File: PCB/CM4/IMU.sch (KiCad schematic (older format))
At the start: 1 part, among them U1 MPU6050

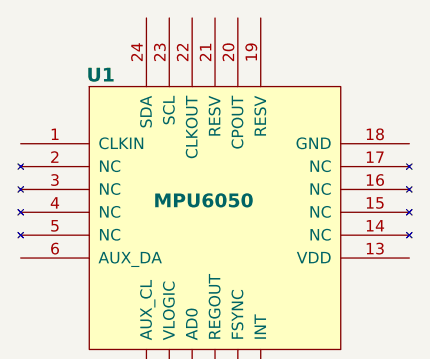
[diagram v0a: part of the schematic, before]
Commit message: Cortex M4 hasbeen placed, decoupling Caps too
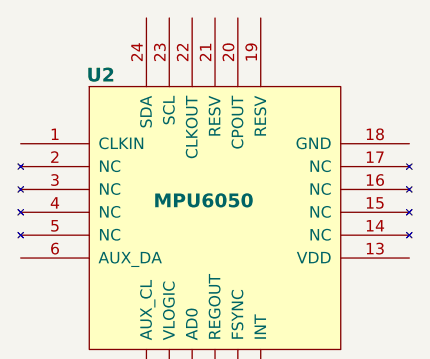
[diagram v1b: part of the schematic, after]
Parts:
- renumbered U1 to U2
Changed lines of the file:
@@
-EESchema Schematic File Version 2  date Fri 02 Nov 2012 01:03:51 PM COT
+EESchema Schematic File Version 2  date Sat 03 Nov 2012 06:00:55 PM COT
 LIBS:power
 LIBS:device
@@
 LIBS:mpu6050
 LIBS:stm32f100vxx
-EELAYER 43  0
+LIBS:HackBo_DroneCore_CM4-cache
+EELAYER 25  0
 EELAYER END
 $Descr A4 11693 8268
 encoding utf-8
-Sheet 2 2
+Sheet 2 3
 Title ""
-Date "2 nov 2012"
+Date "3 nov 2012"
 Rev ""
 Comp ""
@@
 $EndDescr
 $Comp
-L MPU6050 U1
+L MPU6050 U2
 U 1 1 50940AF0
 P 5400 3400
-F 0 "U1" H 4950 3950 60  0000 C CNB
+F 0 "U2" H 4950 3950 60  0000 C CNB
 F 1 "MPU6050" H 5400 3400 60  0000 C CNB
 F 2 "QFN24P" H 5400 3400 60  0001 C CNN

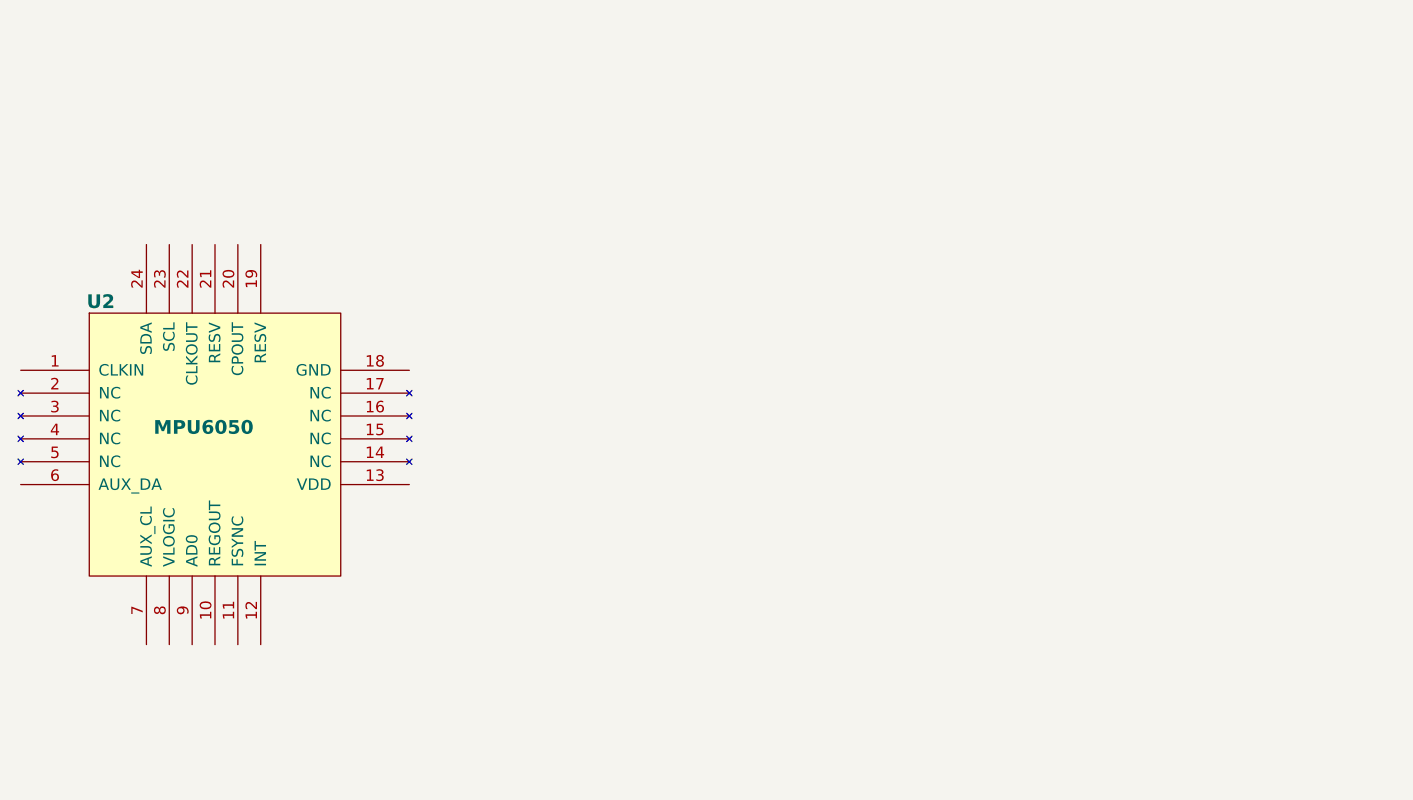
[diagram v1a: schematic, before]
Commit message: IMU caps decoupling
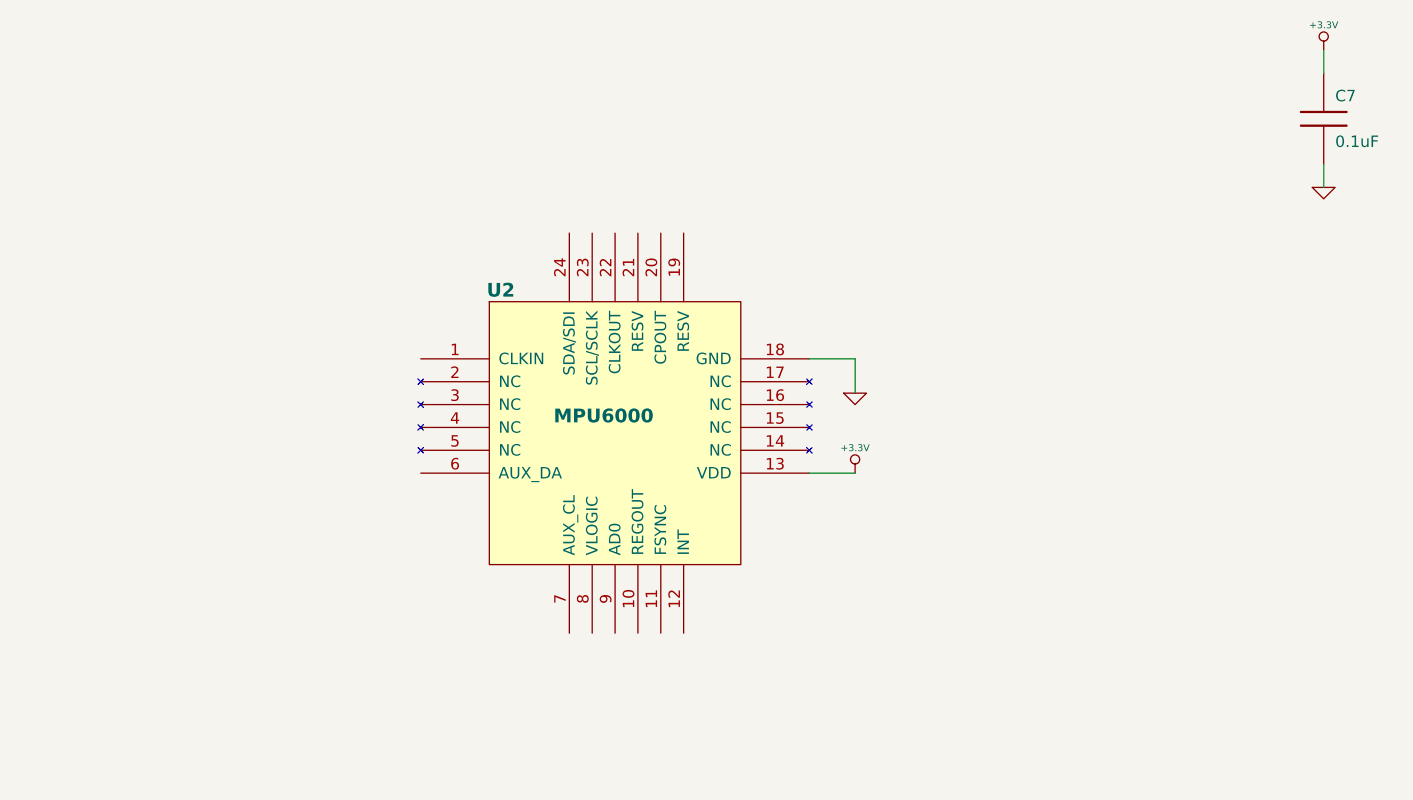
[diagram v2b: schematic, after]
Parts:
- removed U2: MPU6050, QFN24P, symbol MPU6050
- added C7: 0.1uF, 0603, symbol C
- added U2: MPU6000, QFN24P, symbol MPU6000
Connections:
- new net +3.3V: C7.1, U2.13 (VDD)
- new net GND: C7.2, U2.18 (GND)
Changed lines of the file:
@@
-EESchema Schematic File Version 2  date Sat 03 Nov 2012 06:00:55 PM COT
+EESchema Schematic File Version 2  date Sat 03 Nov 2012 06:26:30 PM COT
 LIBS:power
 LIBS:device
@@
 LIBS:mpu6050
 LIBS:stm32f100vxx
+LIBS:mpu6000
 LIBS:HackBo_DroneCore_CM4-cache
 EELAYER 25  0
@@
 $EndDescr
 $Comp
-L MPU6050 U2
-U 1 1 50940AF0
-P 5400 3400
-F 0 "U2" H 4950 3950 60  0000 C CNB
-F 1 "MPU6050" H 5400 3400 60  0000 C CNB
-F 2 "QFN24P" H 5400 3400 60  0001 C CNN
-	1    5400 3400
+L MPU6000 U2
+U 1 1 5095AB32
+P 7150 3350
+F 0 "U2" H 6700 3900 60  0000 C CNB
+F 1 "MPU6000" H 7150 3350 60  0000 C CNB
+F 2 "QFN24P" H 7150 3350 60  0001 C CNN
+	1    7150 3350
 	1    0    0    -1
 $EndComp
+$Comp
+L +3.3V #PWR2
+U 1 1 5095AC9D
+P 8250 3600
+F 0 "#PWR2" H 8250 3560 30  0001 C CNN
+F 1 "+3.3V" H 8250 3710 30  0000 C CNN
+	1    8250 3600
+	1    0    0    -1
+$EndComp
+$Comp
+L GND #PWR4
+U 1 1 5095ACAC
+P 10300 2350
+F 0 "#PWR4" H 10300 2350 30  0001 C CNN
+F 1 "GND" H 10300 2280 30  0001 C CNN
+	1    10300 2350
+	1    0    0    -1
+$EndComp
+$Comp
+L GND #PWR1
+U 1 1 5095ACB9
+P 8250 3250
+F 0 "#PWR1" H 8250 3250 30  0001 C CNN
+F 1 "GND" H 8250 3180 30  0001 C CNN
+	1    8250 3250
+	1    0    0    -1
+$EndComp
+$Comp
+L C C7
+U 1 1 5095ACC1
+P 10300 2050
+F 0 "C7" H 10350 2150 50  0000 L CNN
+F 1 "0.1uF" H 10350 1950 50  0000 L CNN
+F 2 "0603" H 10300 2050 60  0001 C CNN
+	1    10300 2050
+	1    0    0    -1
+$EndComp
+$Comp
+L +3.3V #PWR3
+U 1 1 5095ACEB
+P 10300 1750
+F 0 "#PWR3" H 10300 1710 30  0001 C CNN
+F 1 "+3.3V" H 10300 1860 30  0000 C CNN
+	1    10300 1750
+	1    0    0    -1
+$EndComp
+Wire Wire Line
+	10300 1750 10300 1850
+Wire Wire Line
+	10300 2250 10300 2350
+Wire Wire Line
+	8250 3250 8250 3100
+Wire Wire Line
+	8250 3100 8050 3100
+Wire Wire Line
+	8050 3600 8250 3600
 $EndSCHEMATC

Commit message: IMU caps decoupling
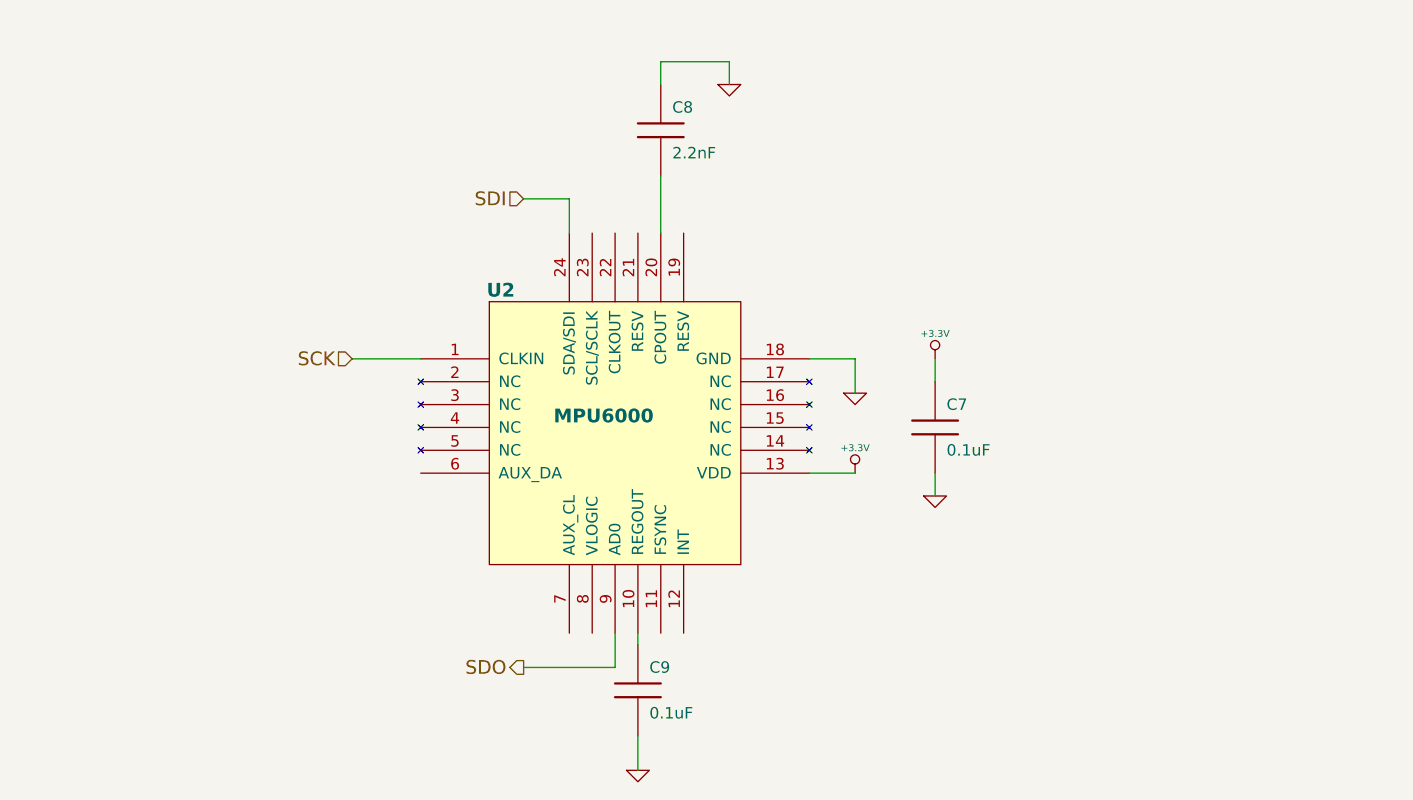
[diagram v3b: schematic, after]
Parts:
- added C8: 2.2nF, 0603, symbol C
- added C9: 0.1uF, 0603, symbol C
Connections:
- net GND: now also C8.1, C9.2
- net SCK: now reaches U2.1 (CLKIN)
- net at U2.10 (REGOUT): now also C9.1
- net at U2.20 (CPOUT): now also C8.2
- net SDI: now reaches U2.24 (SDA/SDI)
- net SDO: now reaches U2.9 (AD0)
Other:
- moved on the sheet: C7
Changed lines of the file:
@@
-EESchema Schematic File Version 2  date Sat 03 Nov 2012 06:26:30 PM COT
+EESchema Schematic File Version 2  date Sat 03 Nov 2012 06:56:08 PM COT
 LIBS:power
 LIBS:device
@@
 $EndComp
 $Comp
-L +3.3V #PWR2
+L +3.3V #PWR4
 U 1 1 5095AC9D
 P 8250 3600
-F 0 "#PWR2" H 8250 3560 30  0001 C CNN
+F 0 "#PWR4" H 8250 3560 30  0001 C CNN
 F 1 "+3.3V" H 8250 3710 30  0000 C CNN
 	1    8250 3600
@@
 $EndComp
 $Comp
-L GND #PWR4
+L GND #PWR6
 U 1 1 5095ACAC
-P 10300 2350
-F 0 "#PWR4" H 10300 2350 30  0001 C CNN
-F 1 "GND" H 10300 2280 30  0001 C CNN
-	1    10300 2350
+P 8600 3700
+F 0 "#PWR6" H 8600 3700 30  0001 C CNN
+F 1 "GND" H 8600 3630 30  0001 C CNN
+	1    8600 3700
 	1    0    0    -1
 $EndComp
 $Comp
-L GND #PWR1
+L GND #PWR3
 U 1 1 5095ACB9
 P 8250 3250
-F 0 "#PWR1" H 8250 3250 30  0001 C CNN
+F 0 "#PWR3" H 8250 3250 30  0001 C CNN
 F 1 "GND" H 8250 3180 30  0001 C CNN
 	1    8250 3250
@@
 L C C7
 U 1 1 5095ACC1
-P 10300 2050
-F 0 "C7" H 10350 2150 50  0000 L CNN
-F 1 "0.1uF" H 10350 1950 50  0000 L CNN
-F 2 "0603" H 10300 2050 60  0001 C CNN
-	1    10300 2050
+P 8600 3400
+F 0 "C7" H 8650 3500 50  0000 L CNN
+F 1 "0.1uF" H 8650 3300 50  0000 L CNN
+F 2 "0603" H 8600 3400 60  0001 C CNN
+	1    8600 3400
 	1    0    0    -1
 $EndComp
 $Comp
-L +3.3V #PWR3
+L +3.3V #PWR5
 U 1 1 5095ACEB
-P 10300 1750
-F 0 "#PWR3" H 10300 1710 30  0001 C CNN
-F 1 "+3.3V" H 10300 1860 30  0000 C CNN
-	1    10300 1750
+P 8600 3100
+F 0 "#PWR5" H 8600 3060 30  0001 C CNN
+F 1 "+3.3V" H 8600 3210 30  0000 C CNN
+	1    8600 3100
 	1    0    0    -1
 $EndComp
 Wire Wire Line
-	10300 1750 10300 1850
+	8600 3100 8600 3200
 Wire Wire Line
-	10300 2250 10300 2350
+	8600 3600 8600 3700
 Wire Wire Line
 	8250 3250 8250 3100
@@
 Wire Wire Line
 	8050 3600 8250 3600
+$Comp
+L C C8
+U 1 1 5095AEE2
+P 7400 2100
+F 0 "C8" H 7450 2200 50  0000 L CNN
+F 1 "2.2nF" H 7450 2000 50  0000 L CNN
+F 2 "0603" H 7400 2100 60  0001 C CNN
+	1    7400 2100
+	1    0    0    -1
+$EndComp
+Wire Wire Line
+	7400 1800 7400 1900
+$Comp
+L GND #PWR2
+U 1 1 5095AEE9
+P 7700 1900
+F 0 "#PWR2" H 7700 1900 30  0001 C CNN
+F 1 "GND" H 7700 1830 30  0001 C CNN
+	1    7700 1900
+	1    0    0    -1
+$EndComp
+Wire Wire Line
+	7700 1800 7700 1900
+Wire Wire Line
+	7400 2300 7400 2550
+Wire Wire Line
+	7400 1800 7700 1800
+$Comp
+L C C9
+U 1 1 5095AFAF
+P 7300 4550
+F 0 "C9" H 7350 4650 50  0000 L CNN
+F 1 "0.1uF" H 7350 4450 50  0000 L CNN
+F 2 "0603" H 7300 4550 60  0001 C CNN
+	1    7300 4550
+	1    0    0    -1
+$EndComp
+$Comp
+L GND #PWR1
+U 1 1 5095AFB5
+P 7300 4900
+F 0 "#PWR1" H 7300 4900 30  0001 C CNN
+F 1 "GND" H 7300 4830 30  0001 C CNN
+	1    7300 4900
+	1    0    0    -1
+$EndComp
+Wire Wire Line
+	7300 4900 7300 4750
+Wire Wire Line
+	7300 4300 7300 4350
+Text HLabel 6800 2400 0    60   Input ~ 0
+SDI
+Text HLabel 6050 3100 0    60   Input ~ 0
+SCK
+Text HLabel 6800 4450 0    60   Output ~ 0
+SDO
+Wire Wire Line
+	7200 4300 7200 4450
+Wire Wire Line
+	7200 4450 6800 4450
+Wire Wire Line
+	6350 3100 6050 3100
+Wire Wire Line
+	7000 2550 7000 2400
+Wire Wire Line
+	7000 2400 6800 2400
 $EndSCHEMATC
